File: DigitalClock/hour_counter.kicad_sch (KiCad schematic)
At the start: 3 parts

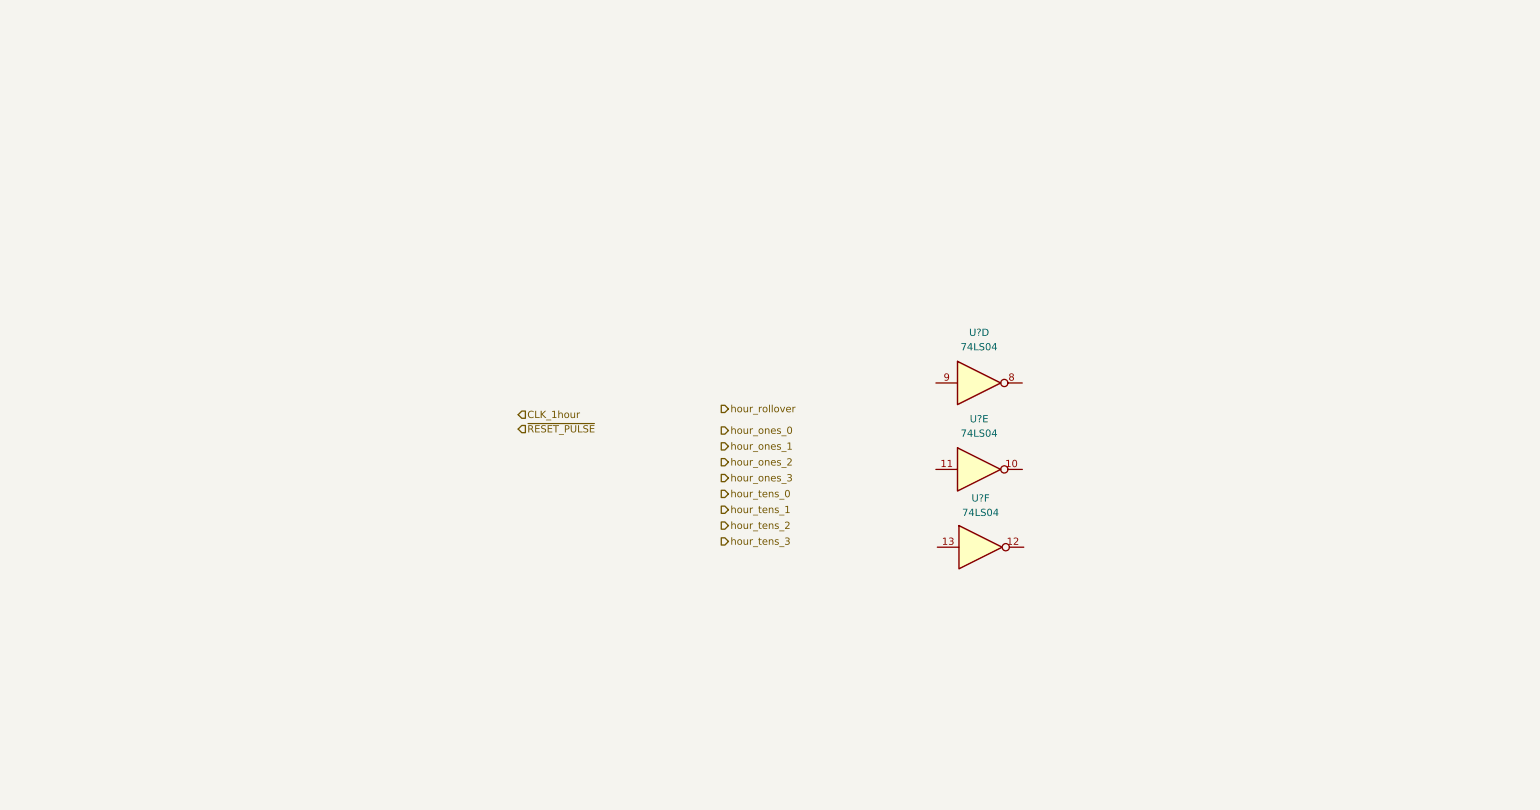
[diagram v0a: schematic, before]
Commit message: added minute counter schematic"
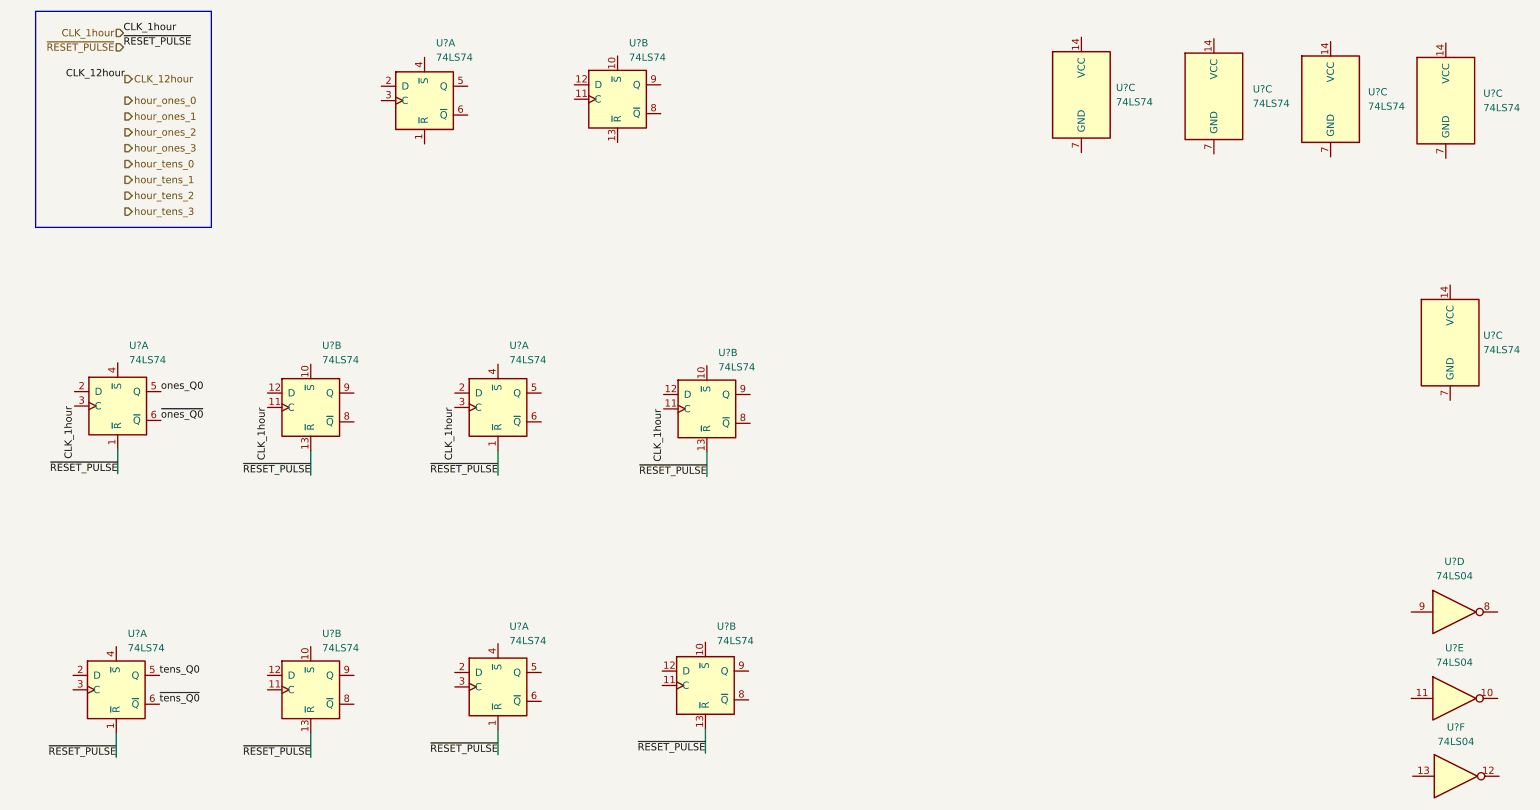
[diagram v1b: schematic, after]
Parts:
- added U? (x15): 74LS74, symbol 74xx:74LS74
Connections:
- net CLK_1hour: now also U?.11 (C), U?.11 (C), U?.3 (C), U?.3 (C)
- net ~{RESET_PULSE}: now also U?.1 (~{R}), U?.1 (~{R}), U?.1 (~{R}), U?.1 (~{R}), U?.13 (~{R}), U?.13 (~{R}), U?.13 (~{R}), U?.13 (~{R})
- new net ones_Q0: U?.5 (Q)
- new net tens_Q0: U?.5 (Q)
- new net ~{ones_Q0}: U?.6 (~{Q})
- new net ~{tens_Q0}: U?.6 (~{Q})
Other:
- moved on the sheet: U?D, U?E, U?F

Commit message: finished kicad schematic
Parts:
- added U39, U44: 74LS86, symbol 74xx:74LS86
- added U42, U43, U47, U48, U51, U53: 74LS08, symbol 74xx:74LS08
- added U49, U50, U52: 74LS32, symbol 74xx:74LS32
- gave numbers to parts that had none: 6
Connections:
- net ones_Q0 is gone; now on net hour_ones_0: U38.5 (Q)
- net CLK_12hour: now also U41.9 (Q)
- net CLK_1hour: now also U41.11 (C), U41.3 (C)
- net hour_ones_0: now also U39.1, U42.1, U47.1, U49.1, U51.1, U51.9
- net hour_ones_1: now also U50.3
- net hour_ones_2: now also U45.5 (Q), U39.5, U42.5, U49.4
- net hour_ones_3: now also U45.9 (Q), U39.10, U49.5, U51.13
- net hour_tens_0: now also U52.6
- net hour_tens_1: now also U40.9 (Q), U43.10, U44.2, U50.10
- net hour_tens_2: now also U46.5 (Q), U43.13, U44.10, U44.5, U49.12
- net hour_tens_3: now also U46.9 (Q), U49.13
- net tens_Q0: now also U43.9, U44.1, U50.9, U52.4
- net ~{ones_Q0}: now also U43.1
- net ~{tens_Q0}: now also U48.1
- net tens_D2: now reaches U46.2 (D)
- net tens_D2: now also U47.8
- net CLK_10hour: now reaches U46.3 (C)
- net CLK_10hour: now also U40.11 (C), U40.3 (C), U41.5 (Q), U46.11 (C)
- net +5V: now reaches U46.4 (~{S})
- net +5V: now also U38.10 (~{S}), U38.14 (VCC), U38.4 (~{S}), U40.10 (~{S}), U40.14 (VCC), U40.4 (~{S}), U41.1 (~{R}), U41.10 (~{S}), U41.13 (~{R}), U41.14 (VCC), U41.4 (~{S}), U45.10 (~{S}), U45.14 (VCC), U45.4 (~{S}), U46.10 (~{S}), U46.14 (VCC), U39.14 (VCC), U42.14 (VCC), U43.14 (VCC), U44.14 (VCC), U47.14 (VCC), U48.14 (VCC), U49.14 (VCC), U50.14 (VCC), U51.14 (VCC), U52.14 (VCC), U53.14 (VCC)
- net ~{tens_Q2}: now reaches U46.6 (~{Q})
- net GND: now reaches U41.7 (GND)
- net GND: now also U38.7 (GND), U40.7 (GND), U45.7 (GND), U46.7 (GND), U39.12, U39.13, U39.7 (GND), U42.7 (GND), U43.7 (GND), U44.12, U44.13, U44.7 (GND), U47.7 (GND), U48.7 (GND), U49.7 (GND), U50.7 (GND), U51.7 (GND), U52.12, U52.13, U52.7 (GND), U53.10, U53.12, U53.13, U53.7 (GND), U53.9
- net =9 or =11?: now reaches U41.2 (D)
- net =9 or =11?: now also U15.13, U49.8
- net tens_D0: now reaches U40.2 (D)
- net tens_D0: now also U48.3
- net ~{=9 or =11?}: now reaches U15.12
- net ~{=9 or =11?}: now also U42.10, U42.13, U43.2, U43.5
- net tens_D3: now reaches U46.12 (D)
- net tens_D3: now also U47.11
- net ~{tens_Q3}: now reaches U46.8 (~{Q})
- net =0?: now reaches U15.8
- net =0?: now also U50.2, U52.5
- net at U15.9: now also U50.11
- net ~{=11?}: now reaches U15.10
- net ~{=11?}: now also U47.10, U47.13, U48.2, U48.5
- net =11?: now reaches U15.11
- net =11?: now also U41.12 (D), U48.11, U49.9
- net ones_D1: now reaches U38.12 (D)
- net ones_D1: now also U43.6
- net ~{ones_Q1}: now reaches U38.8 (~{Q})
- net ~{ones_Q1}: now also U47.2, U51.10, U51.2
- net ones_Q1: now reaches U38.9 (Q)
- net ones_Q1: now also U39.2, U42.2, U49.2, U50.1
- net ones_D3: now reaches U45.12 (D)
- net ones_D3: now also U42.11
- net ~{ones_Q3}: now reaches U45.8 (~{Q})
- net ~{ones_Q3}: now also U47.5, U51.5
- net ones_D0: now reaches U38.2 (D)
- net ones_D0: now also U43.3
- net tens_D1: now reaches U40.12 (D)
- net tens_D1: now also U48.6
- net ~{tens_Q1}: now reaches U40.8 (~{Q})
- net ones_D2: now reaches U45.2 (D)
- net ones_D2: now also U42.8
- net ~{ones_Q2}: now reaches U45.6 (~{Q})
- net ~{ones_Q2}: now also U47.4, U51.12, U51.4
- new net: U47.6, U48.10
- new net: U44.3, U48.4
- new net: U39.8, U42.12
- new net: U44.6, U47.9
- new net: U49.11, U52.10
- new net: U50.13, U52.8
- new net: U50.8, U52.9
- new net: U39.6, U42.9
- new net: U51.3, U53.1
- new net: U51.6, U53.2
- new net: U49.6, U50.5
- new net: U49.3, U50.4
- new net: U50.12, U50.6
- new net: U51.8, U53.4
- new net: U44.8, U47.12
- new net: U39.3, U43.4
- new net: U51.11, U53.5
- new net: U47.3, U48.9
- new net: U48.12, U48.8
- new net =1?: U48.13, U53.3
- new net =9?: U49.10, U53.6
- new net ones_Q01: U39.4, U42.3, U42.4
- new net ones_Q012: U39.9, U42.6
- new net tens_Q01: U43.12, U43.8, U44.4
- new net tens_Q012: U43.11, U44.9
- no-connect marks 0 -> 7
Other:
- note added: "If output = 00, display 12 instead. So 0000 0000 becomes 0001 0010."
- moved on the sheet: U15D, U15E, U15F, U38A, U38B, U38C, U40A, U40B, U40C, U41A, U41B, U41C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

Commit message: about to begin layout
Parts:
- added unit 1 of U52
- U15, U38, U39, U40, U41, U42, U43, U44, U45, U46, U47, U48, U49, U50, U51, U52, U53: footprint (none) -> Package_DIP:DIP-14_W7.62mm
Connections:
- net =0?: now also U52.10; no longer U50.2
- net =11?: now also U52.1; no longer U49.9
- net =9 or =11?: now also U52.3; no longer U49.8
- net =9?: now also U52.2; no longer U49.10
- net GND: now also U50.10, U50.9
- net hour_ones_1: now also U52.6; no longer U50.3
- net hour_tens_0: now also U52.8; no longer U52.6
- net hour_tens_1: now also U49.10; no longer U50.10
- net ones_Q1: now also U52.4; no longer U50.1
- net tens_Q0: now also U49.9, U52.9; no longer U50.9, U52.4
- net at U49.11: now also U50.2; no longer U52.10
- net at U50.13: now also U50.3; no longer U52.8
- net at U50.8: no longer U52.9
- new net: U49.8, U50.1
- no-connect marks 7 -> 8
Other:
- moved on the sheet: U39D, U44D, U49C, U50A, U50C

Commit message: started routing
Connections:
- net =1?: now also U51.8; no longer U53.3
- net =9?: now also U53.8; no longer U53.6
- net GND: now also U50.12, U50.13, U51.12, U51.13; no longer U50.10, U50.9, U53.10, U53.9
- net hour_ones_0: now also U48.1, U53.1; no longer U47.1, U51.9
- net hour_ones_3: now also U53.5; no longer U51.13
- net hour_tens_1: now also U42.10; no longer U43.10
- net hour_tens_2: now also U42.13; no longer U43.13
- net ones_D2: now also U43.8; no longer U42.8
- net ones_D3: now also U43.11; no longer U42.11
- net tens_D0: now also U47.3; no longer U48.3
- net tens_D1: now also U47.6; no longer U48.6
- net tens_Q0: now also U42.9; no longer U43.9
- net tens_Q01: now also U42.12, U42.8; no longer U43.12, U43.8
- net tens_Q012: now also U42.11; no longer U43.11
- net ~{=11?}: now also U47.2, U47.5; no longer U48.2, U48.5
- net ~{=9 or =11?}: now also U43.10, U43.13; no longer U42.10, U42.13
- net ~{ones_Q1}: now also U48.2, U53.2; no longer U47.2, U51.10
- net ~{ones_Q2}: now also U48.4, U53.4; no longer U47.4, U51.12
- net ~{ones_Q3}: now also U48.5; no longer U47.5
- net ~{tens_Q0}: now also U47.1; no longer U48.1
- net at U48.10: now also U48.6; no longer U47.6
- net at U44.3: now also U47.4; no longer U48.4
- net at U39.8: now also U43.12; no longer U42.12
- net at U15.9: now also U50.8; no longer U50.11
- net at U39.6: now also U43.9; no longer U42.9
- net at U51.3: now also U51.9; no longer U53.1
- net at U51.6: now also U51.10; no longer U53.2
- net at U50.6: now also U50.9; no longer U50.12
- net at U51.11: no longer U53.5
- net at U48.9: now also U48.3; no longer U47.3
- net at U50.3: now also U50.10; no longer U50.13
- new net: U53.3, U53.9
- new net: U53.10, U53.6
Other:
- moved on the sheet: U42C, U42D, U43C, U43D, U47A, U47B, U48A, U48B, U50C, U50D, U51C, U51D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
